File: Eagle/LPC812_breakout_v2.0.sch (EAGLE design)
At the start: 11 parts

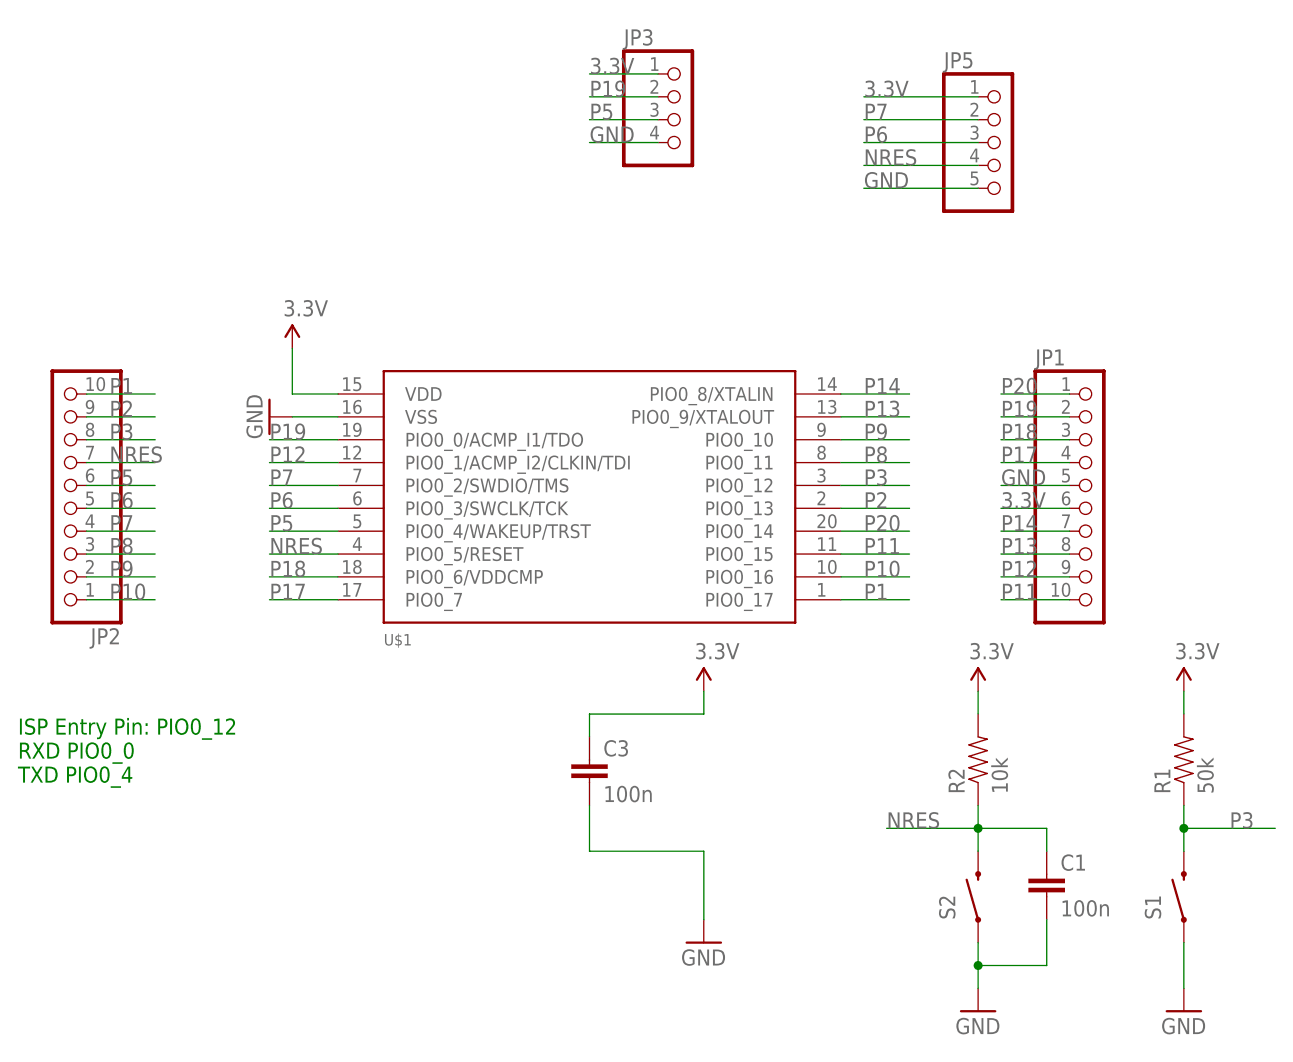
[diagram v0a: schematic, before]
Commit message: Revision 2
Changes:

- 10 mil traces, no 90° bends, ground plane where possible.
- Font size for pin labelling increased.
- Removed SWD port to reduce complexity and size. If needed, the board
can be accessed at the broken out pins.
- Included 3.3V regulator, since the driving ability of those includede
in the USB to serial converters is limited.
- Removed debouncing cap from reset switch.
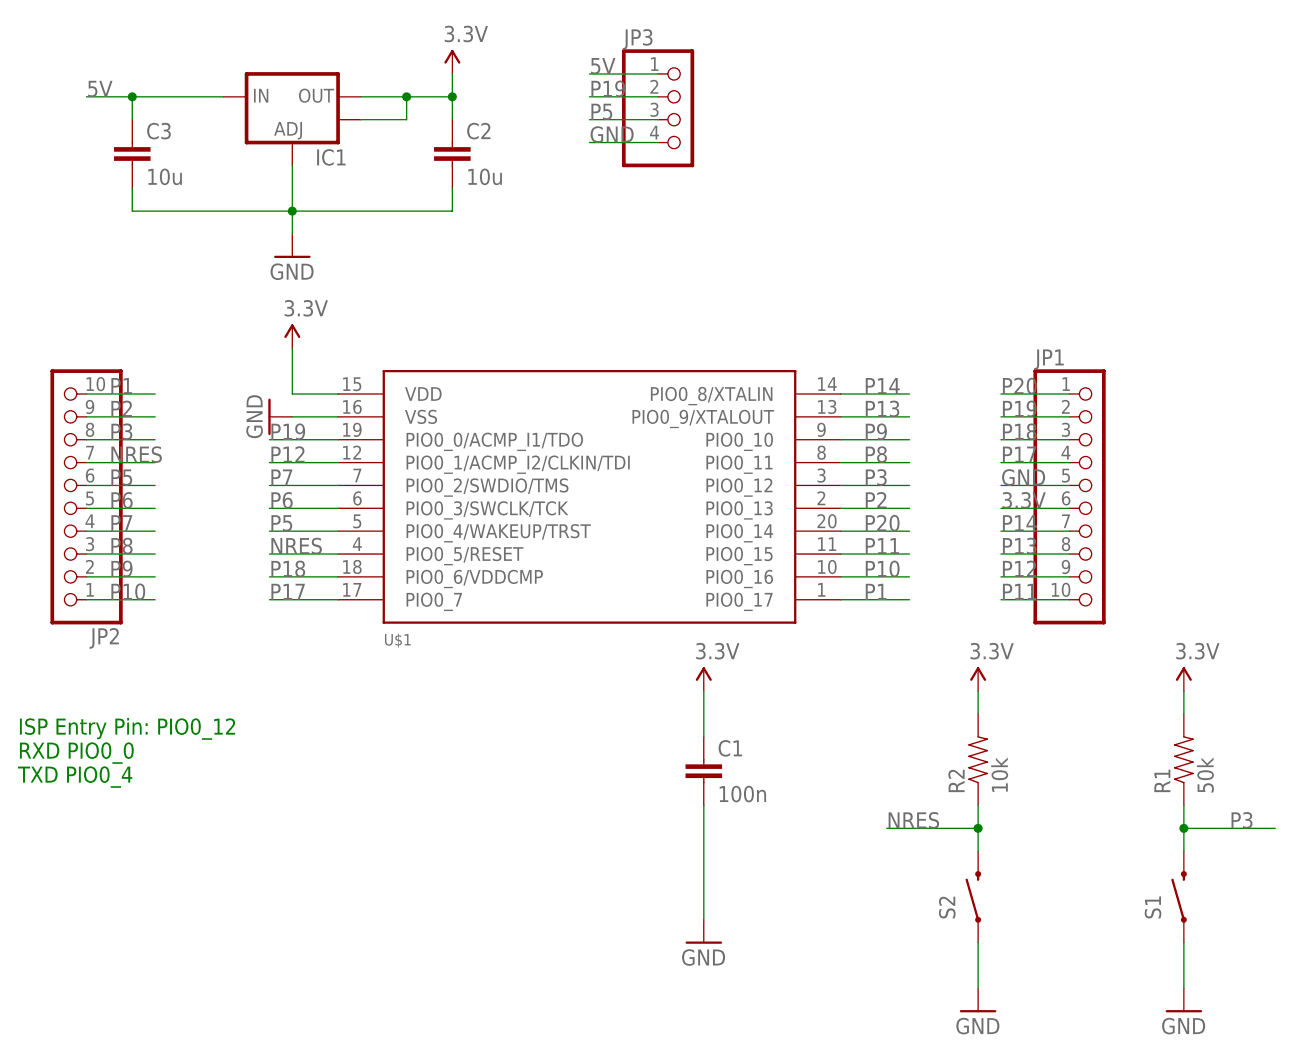
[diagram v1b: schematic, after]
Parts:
- removed JP5: (no value), microbuilder:HEADER-1X5ROUND
- added C2: 10u, SparkFun-Capacitors:CAP0805
- added IC1: (no value), SparkFun-PowerIC:V_REG_LM1117SOT223
- C3: value 100n -> 10u
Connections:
- new net 5V: C3.1, IC1.IN, JP3.1
- net 3.3V: now also C1.1, C2.1, IC1.OUT, IC1.OUT@1; no longer C3.1, JP3.1, JP5.1
- net GND: now also C2.2, IC1.ADJ; no longer JP5.5
- net NRES: no longer C1.1, JP5.4
- net P6: no longer JP5.3
- net P7: no longer JP5.2
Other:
- moved on the sheet: C1, C3
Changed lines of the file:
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@@
 </variantdefs>
 <classes>
-<class number="0" name="default" width="0" drill="0">
+<class number="0" name="default" width="0.254" drill="0">
+<clearance class="0" value="0.2032"/>
 </class>
 </classes>
@@
 <part name="JP1" library="microbuilder" deviceset="HEADER-1X10" device="ROUND"/>
 <part name="JP2" library="microbuilder" deviceset="HEADER-1X10" device="ROUND"/>
-<part name="C1" library="SparkFun-Capacitors" deviceset="CAP" device="0805" value="100n"/>
 <part name="R1" library="SparkFun-Resistors" deviceset="RESISTOR" device="0805-RES" value="50k"/>
 <part name="R2" library="SparkFun-Resistors" deviceset="RESISTOR" device="0805-RES" value="10k"/>
 <part name="S1" library="SparkFun-Electromechanical" deviceset="SWITCH-MOMENTARY-2" device="-SMD-1101NE"/>
 <part name="S2" library="SparkFun-Electromechanical" deviceset="SWITCH-MOMENTARY-2" device="-SMD-1101NE"/>
-<part name="C3" library="SparkFun-Capacitors" deviceset="CAP" device="0805" value="100n"/>
+<part name="C1" library="SparkFun-Capacitors" deviceset="CAP" device="0805" value="100n"/>
 <part name="JP3" library="microbuilder" deviceset="HEADER-1X4" device="ROUND"/>
-<part name="JP5" library="microbuilder" deviceset="HEADER-1X5" device="ROUND"/>
 <part name="GND1" library="SparkFun-Aesthetics" deviceset="GND" device=""/>
 <part name="GND2" library="SparkFun-Aesthetics" deviceset="GND" device=""/>
@@
 <part name="GND5" library="SparkFun-Aesthetics" deviceset="GND" device=""/>
 <part name="SUPPLY7" library="SparkFun-Aesthetics" deviceset="3.3V" device=""/>
+<part name="IC1" library="SparkFun-PowerIC" deviceset="V_REG_LM1117" device="SOT223"/>
+<part name="C2" library="SparkFun-Capacitors" deviceset="CAP" device="0805" value="10u"/>
+<part name="C3" library="SparkFun-Capacitors" deviceset="CAP" device="0805" value="10u"/>
+<part name="GND4" library="SparkFun-Aesthetics" deviceset="GND" device=""/>
+<part name="SUPPLY4" library="SparkFun-Aesthetics" deviceset="3.3V" device=""/>
 </parts>
 <sheets>
@@
 <instance part="JP1" gate="A" x="106.68" y="50.8"/>
 <instance part="JP2" gate="A" x="-7.62" y="48.26" rot="R180"/>
-<instance part="C1" gate="G$1" x="101.6" y="5.08"/>
 <instance part="R1" gate="G$1" x="116.84" y="20.32" rot="R90"/>
 <instance part="R2" gate="G$1" x="93.98" y="20.32" rot="R90"/>
@@
 <attribute name="NAME" x="91.44" y="2.54" size="1.778" layer="95" rot="R90"/>
 </instance>
-<instance part="C3" gate="G$1" x="50.8" y="17.78"/>
+<instance part="C1" gate="G$1" x="63.5" y="17.78"/>
 <instance part="JP3" gate="A" x="60.96" y="91.44"/>
-<instance part="JP5" gate="A" x="96.52" y="88.9"/>
 <instance part="GND1" gate="1" x="116.84" y="-7.62"/>
 <instance part="GND2" gate="1" x="93.98" y="-7.62"/>
@@
 <instance part="GND5" gate="1" x="15.24" y="58.42" rot="R270"/>
 <instance part="SUPPLY7" gate="G$1" x="17.78" y="66.04"/>
+<instance part="IC1" gate="G$1" x="17.78" y="93.98"/>
+<instance part="C2" gate="G$1" x="35.56" y="86.36"/>
+<instance part="C3" gate="G$1" x="0" y="86.36"/>
+<instance part="GND4" gate="1" x="17.78" y="76.2"/>
+<instance part="SUPPLY4" gate="G$1" x="35.56" y="96.52"/>
 </instances>
 <busses>
@@
 </segment>
 <segment>
-<pinref part="C3" gate="G$1" pin="1"/>
-<wire x1="50.8" y1="22.86" x2="50.8" y2="25.4" width="0.1524" layer="91"/>
+<pinref part="C1" gate="G$1" pin="1"/>
 <pinref part="SUPPLY3" gate="G$1" pin="3.3V"/>
-<wire x1="50.8" y1="25.4" x2="63.5" y2="25.4" width="0.1524" layer="91"/>
-<wire x1="63.5" y1="27.94" x2="63.5" y2="25.4" width="0.1524" layer="91"/>
+<wire x1="63.5" y1="27.94" x2="63.5" y2="22.86" width="0.1524" layer="91"/>
 </segment>
 <segment>
@@
 </segment>
 <segment>
-<pinref part="JP3" gate="A" pin="1"/>
-<wire x1="58.42" y1="96.52" x2="50.8" y2="96.52" width="0.1524" layer="91"/>
-<label x="50.8" y="96.52" size="1.778" layer="95"/>
-</segment>
-<segment>
-<pinref part="JP5" gate="A" pin="1"/>
-<wire x1="93.98" y1="93.98" x2="81.28" y2="93.98" width="0.1524" layer="91"/>
-<label x="81.28" y="93.98" size="1.778" layer="95"/>
+<pinref part="IC1" gate="G$1" pin="OUT"/>
+<wire x1="25.4" y1="93.98" x2="30.48" y2="93.98" width="0.1524" layer="91"/>
+<pinref part="IC1" gate="G$1" pin="OUT@1"/>
+<wire x1="25.4" y1="91.44" x2="30.48" y2="91.44" width="0.1524" layer="91"/>
+<wire x1="30.48" y1="91.44" x2="30.48" y2="93.98" width="0.1524" layer="91"/>
+<junction x="30.48" y="93.98"/>
+<wire x1="30.48" y1="93.98" x2="35.56" y2="93.98" width="0.1524" layer="91"/>
+<pinref part="C2" gate="G$1" pin="1"/>
+<wire x1="35.56" y1="93.98" x2="35.56" y2="91.44" width="0.1524" layer="91"/>
+<pinref part="SUPPLY4" gate="G$1" pin="3.3V"/>
+<wire x1="35.56" y1="96.52" x2="35.56" y2="93.98" width="0.1524" layer="91"/>
+<junction x="35.56" y="93.98"/>
 </segment>
 </net>
@@
 <pinref part="S2" gate="G$1" pin="1"/>
 <pinref part="GND2" gate="1" pin="GND"/>
-<wire x1="93.98" y1="0" x2="93.98" y2="-2.54" width="0.1524" layer="91"/>
-<wire x1="93.98" y1="-2.54" x2="93.98" y2="-5.08" width="0.1524" layer="91"/>
-<wire x1="93.98" y1="-2.54" x2="101.6" y2="-2.54" width="0.1524" layer="91"/>
+<wire x1="93.98" y1="0" x2="93.98" y2="-5.08" width="0.1524" layer="91"/>
+</segment>
+<segment>
+<pinref part="GND3" gate="1" pin="GND"/>
+<wire x1="63.5" y1="2.54" x2="63.5" y2="15.24" width="0.1524" layer="91"/>
 <pinref part="C1" gate="G$1" pin="2"/>
-<wire x1="101.6" y1="-2.54" x2="101.6" y2="2.54" width="0.1524" layer="91"/>
-<junction x="93.98" y="-2.54"/>
-</segment>
-<segment>
-<pinref part="GND3" gate="1" pin="GND"/>
-<wire x1="63.5" y1="2.54" x2="63.5" y2="10.16" width="0.1524" layer="91"/>
-<pinref part="C3" gate="G$1" pin="2"/>
-<wire x1="50.8" y1="15.24" x2="50.8" y2="10.16" width="0.1524" layer="91"/>
-<wire x1="50.8" y1="10.16" x2="63.5" y2="10.16" width="0.1524" layer="91"/>
 </segment>
 <segment>
@@
 </segment>
 <segment>
-<pinref part="JP5" gate="A" pin="5"/>
-<wire x1="93.98" y1="83.82" x2="81.28" y2="83.82" width="0.1524" layer="91"/>
-<label x="81.28" y="83.82" size="1.778" layer="95"/>
+<pinref part="IC1" gate="G$1" pin="ADJ"/>
+<wire x1="17.78" y1="86.36" x2="17.78" y2="81.28" width="0.1524" layer="91"/>
+<pinref part="C3" gate="G$1" pin="2"/>
+<wire x1="0" y1="83.82" x2="0" y2="81.28" width="0.1524" layer="91"/>
+<wire x1="0" y1="81.28" x2="17.78" y2="81.28" width="0.1524" layer="91"/>
+<wire x1="17.78" y1="81.28" x2="35.56" y2="81.28" width="0.1524" layer="91"/>
+<pinref part="C2" gate="G$1" pin="2"/>
+<wire x1="35.56" y1="81.28" x2="35.56" y2="83.82" width="0.1524" layer="91"/>
+<pinref part="GND4" gate="1" pin="GND"/>
+<wire x1="17.78" y1="81.28" x2="17.78" y2="78.74" width="0.1524" layer="91"/>
+<junction x="17.78" y="81.28"/>
 </segment>
 </net>
@@
 <wire x1="93.98" y1="10.16" x2="93.98" y2="12.7" width="0.1524" layer="91"/>
 <wire x1="93.98" y1="12.7" x2="93.98" y2="15.24" width="0.1524" layer="91"/>
-<wire x1="93.98" y1="12.7" x2="101.6" y2="12.7" width="0.1524" layer="91"/>
-<pinref part="C1" gate="G$1" pin="1"/>
-<wire x1="101.6" y1="12.7" x2="101.6" y2="10.16" width="0.1524" layer="91"/>
 <junction x="93.98" y="12.7"/>
 <wire x1="93.98" y1="12.7" x2="83.82" y2="12.7" width="0.1524" layer="91"/>
@@
 <label x="-2.54" y="53.34" size="1.778" layer="95"/>
 </segment>
-<segment>
-<pinref part="JP5" gate="A" pin="4"/>
-<wire x1="93.98" y1="86.36" x2="81.28" y2="86.36" width="0.1524" layer="91"/>
-<label x="81.28" y="86.36" size="1.778" layer="95"/>
-</segment>
 </net>
 <net name="P17" class="0">
@@
 <label x="-2.54" y="48.26" size="1.778" layer="95"/>
 </segment>
-<segment>
-<pinref part="JP5" gate="A" pin="3"/>
-<wire x1="93.98" y1="88.9" x2="81.28" y2="88.9" width="0.1524" layer="91"/>
-<label x="81.28" y="88.9" size="1.778" layer="95"/>
-</segment>
 </net>
 <net name="P7" class="0">
@@
 <wire x1="-5.08" y1="45.72" x2="2.54" y2="45.72" width="0.1524" layer="91"/>
 <label x="-2.54" y="45.72" size="1.778" layer="95"/>
-</segment>
-<segment>
-<pinref part="JP5" gate="A" pin="2"/>
-<wire x1="93.98" y1="91.44" x2="81.28" y2="91.44" width="0.1524" layer="91"/>
-<label x="81.28" y="91.44" size="1.778" layer="95"/>
 </segment>
 </net>
@@
 </segment>
 </net>
+<net name="5V" class="0">
+<segment>
+<pinref part="JP3" gate="A" pin="1"/>
+<wire x1="58.42" y1="96.52" x2="50.8" y2="96.52" width="0.1524" layer="91"/>
+<label x="50.8" y="96.52" size="1.778" layer="95"/>
+</segment>
+<segment>
+<pinref part="IC1" gate="G$1" pin="IN"/>
+<wire x1="10.16" y1="93.98" x2="0" y2="93.98" width="0.1524" layer="91"/>
+<pinref part="C3" gate="G$1" pin="1"/>
+<wire x1="0" y1="93.98" x2="-5.08" y2="93.98" width="0.1524" layer="91"/>
+<wire x1="0" y1="91.44" x2="0" y2="93.98" width="0.1524" layer="91"/>
+<junction x="0" y="93.98"/>
+<label x="-5.08" y="93.98" size="1.778" layer="95"/>
+</segment>
+</net>
